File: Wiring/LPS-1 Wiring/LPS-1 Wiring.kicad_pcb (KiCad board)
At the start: 4 copper layers, 9 parts, among them J1 +12V Connector block, J2 Battery, J4 Solar charging unit, J5 Solar Panel, J6 GND Connector Block], J7 LPS-1 Monitoring Unit, J8 Fuse Block, SW2 Load Monitoring Control, SW3 Battery Kill Switch

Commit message: Chagnes to the panel layout
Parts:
- moved J8 75.8 mm to (644.7, 338.7)
- moved J1 62.3 mm to (586.8, 440.0)
- moved J6 62.3 mm to (607.7, 440.0)
- moved J2 49.0 mm to (537.6, 530.9), turned to -90 degrees
- moved J4 35.5 mm to (557.2, 357.7)
- moved J5 13.1 mm to (563.4, 219.3)
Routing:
- net unconnected-(J6-Pin_2-Pad6): track 219.3 -> 0.00 mm
- net unconnected-(J6-Pin_2-Pad2): track 0.00 -> 201.4 mm
- net /Lamp 11.2W: track 181.4 -> 253.0 mm
- net Net-(SW3B-A): track 111.8 -> 177.0 mm
- net Net-(SW2A-B): track 106.0 -> 168.6 mm
- net Net-(SW3A-A): track 85.9 -> 148.0 mm
- net Net-(J7-Pin_2): track 228.6 -> 277.5 mm
- net Net-(J2-Pin_1): track 110.5 -> 154.4 mm
- net /SP+: track 120.0 -> 145.9 mm
- net Net-(J2-Pin_2): track 166.3 -> 191.8 mm
- net /SP-: track 120.9 -> 144.9 mm
- net Net-(J8-COMM): track 273.7 -> 295.5 mm
- net Net-(J4-Pin_2): track 72.7 -> 93.1 mm
- net Net-(J4-Pin_1): track 79.3 -> 86.5 mm

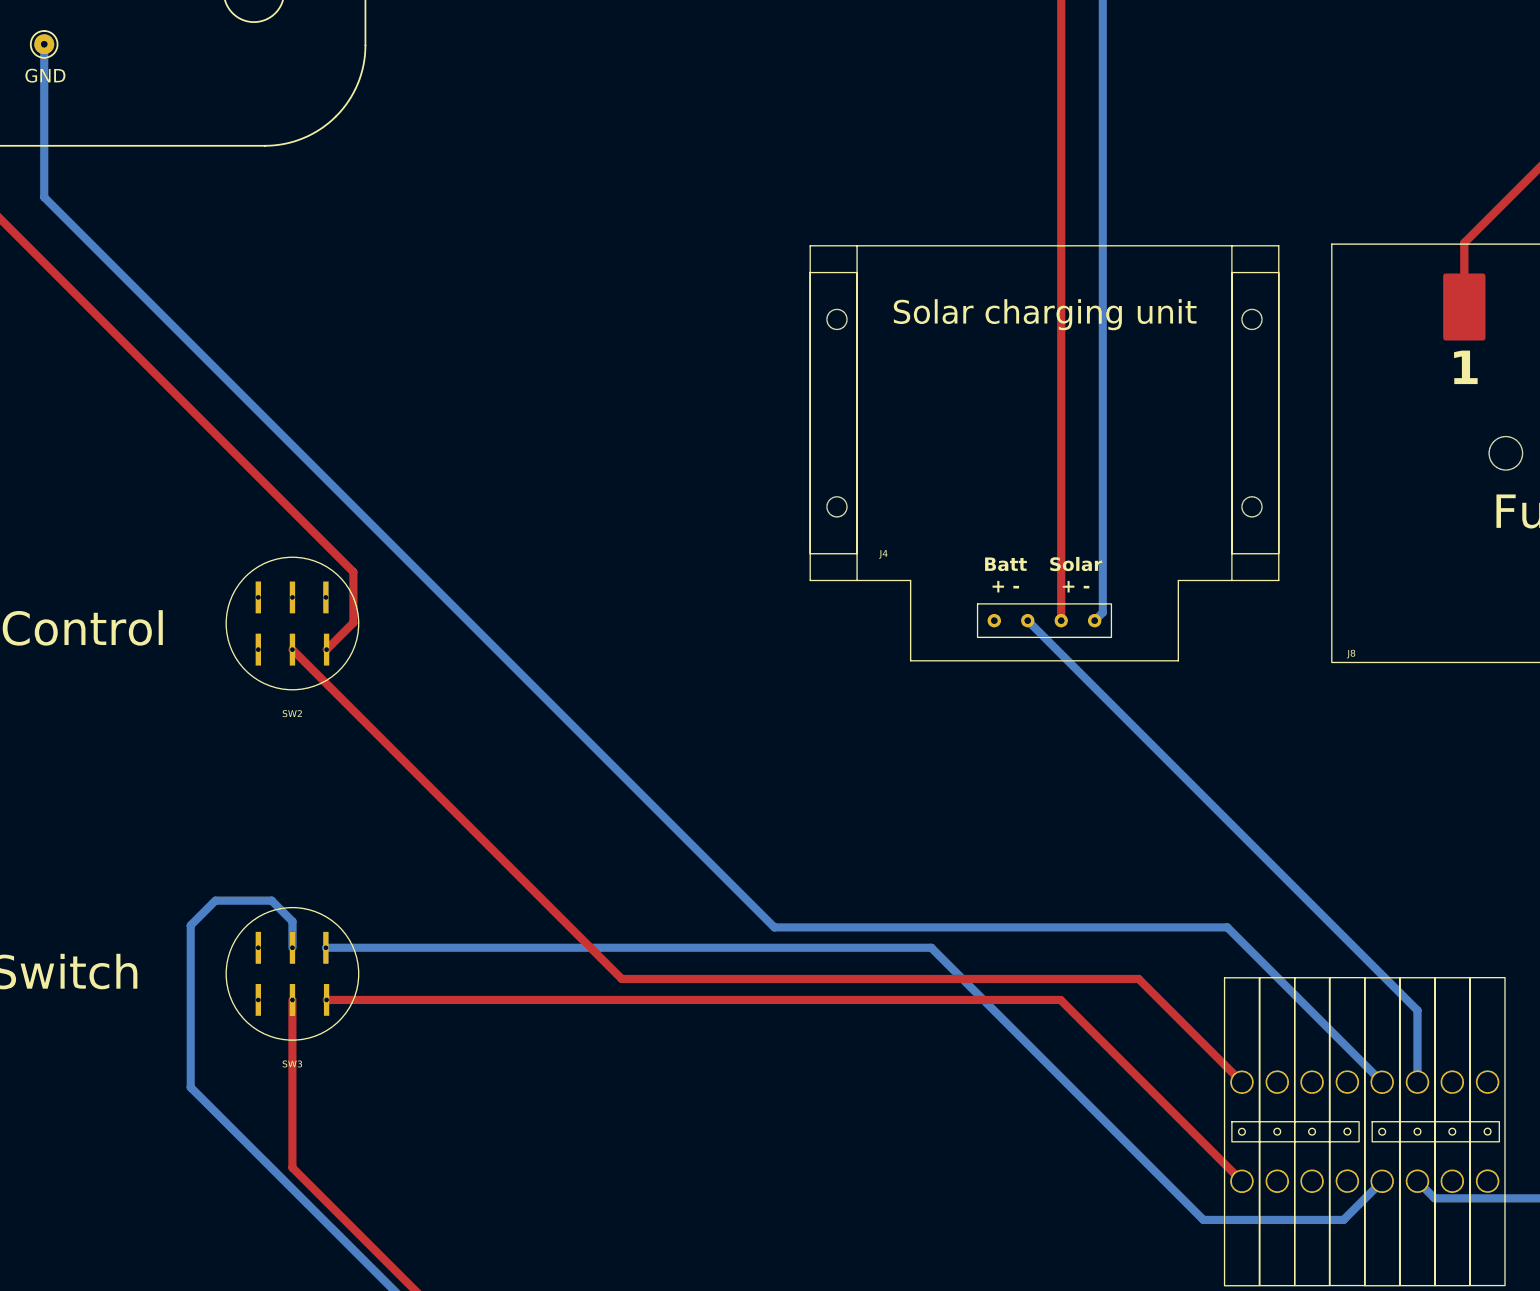
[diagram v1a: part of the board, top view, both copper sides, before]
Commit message: Moved the design to KiCad 10
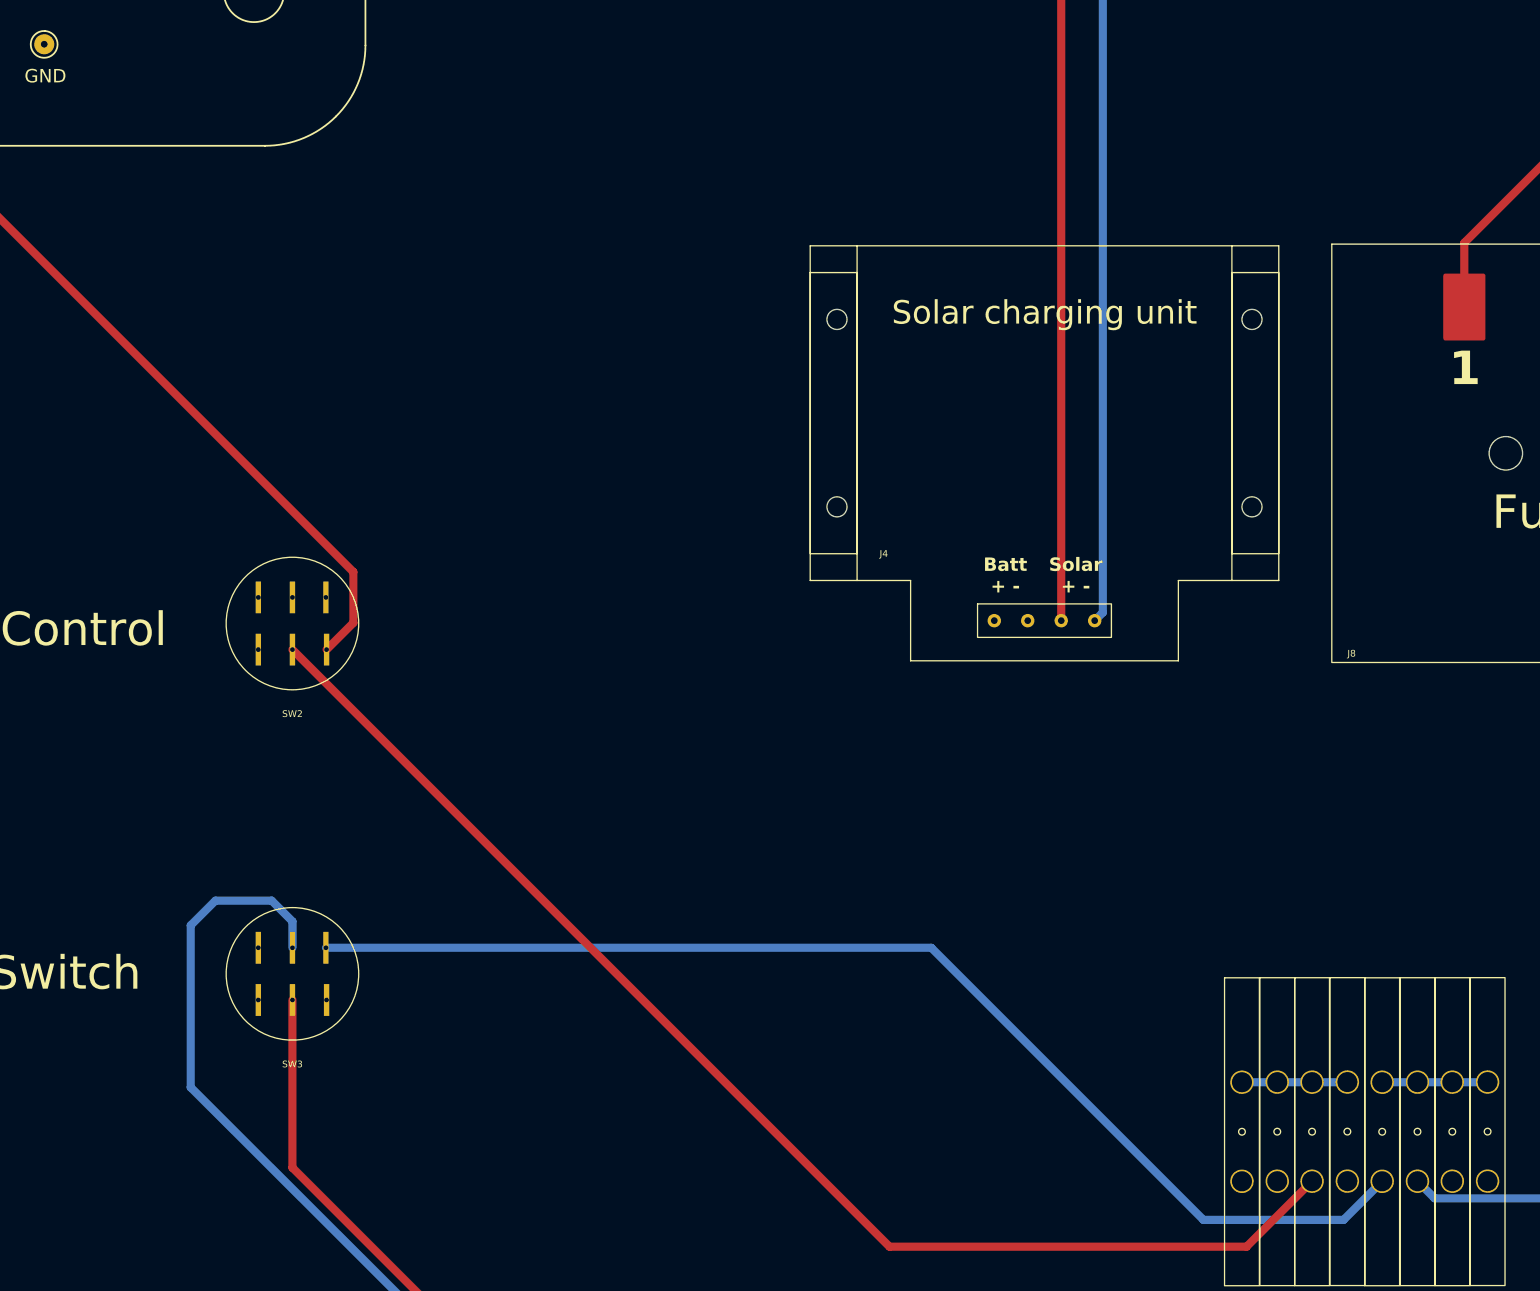
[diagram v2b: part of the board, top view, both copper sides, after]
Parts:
- J1, J6: footprint Wiring:Degson_04_Bridged-PC2.5-01P-11-00AH-1_5.2 -> Wiring:Degson_04_Bridged-PC2.5-01P-11-00AH-1_5.2_H
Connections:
- net /Lamp 11.2W renamed /Lamp +ve
- J1 pad 2: unconnected-(J1-Pin_2-Pad2) -> Net-(J4-Pin_1)
- J1 pad 3: unconnected-(J1-Pin_1-Pad3) -> Net-(SW2A-B)
- J1 pad 5: unconnected-(J1-Pin_1-Pad5) -> Net-(J1-Pin_1-Pad5)
- J1 pad 6: unconnected-(J1-Pin_2-Pad6) -> Net-(J1-Pin_1-Pad5)
- J1 pad 7: Net-(J4-Pin_1) -> Net-(J1-Pin_1-Pad5)
- J1 pad 8: Net-(SW2A-B) -> Net-(J1-Pin_1-Pad5)
- J4 pad 3: /SP+ -> unconnected-(J4-Pin_3-Pad3)
- J6 pad 2: unconnected-(J6-Pin_2-Pad2) -> Net-(J4-Pin_2)
- J6 pad 3: unconnected-(J6-Pin_1-Pad3) -> Net-(J7-Pin_2)
- J6 pad 4: unconnected-(J6-Pin_2-Pad4) -> /Lamp -Ve
- J6 pad 5: unconnected-(J6-Pin_1-Pad5) -> Net-(J6-Pin_1-Pad5)
- J6 pad 6: unconnected-(J6-Pin_2-Pad6) -> Net-(J6-Pin_1-Pad5)
- J6 pad 7: Net-(J4-Pin_2) -> Net-(J6-Pin_1-Pad5)
- J6 pad 8: Net-(J7-Pin_2) -> Net-(J6-Pin_1-Pad5)
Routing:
- net Net-(J4-Pin_2): track 93.1 -> 405.2 mm
- net unconnected-(J6-Pin_2-Pad2): track 201.4 -> 0.00 mm
- net Net-(J7-Pin_2): track 277.5 -> 374.6 mm
- net Net-(J4-Pin_1): track 86.5 -> 133.6 mm
- net Net-(SW2A-B): track 168.6 -> 193.3 mm
- net Net-(J1-Pin_1-Pad5): track 0.00 -> 15.8 mm
- net Net-(J6-Pin_1-Pad5): track 0.00 -> 15.8 mm
- net Net-(SW3A-A): track 148.0 -> 161.9 mm
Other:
- copper layers 4 -> 6

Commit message: Update to the connection block symols and footprints
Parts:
- removed the J6 at (607.7, 440.0)
- added J7: Block_Connector_04_b, Wiring:Degson_04_Bridged-PC2.5-01P-11-00AH-1_5.2, F.Cu at (606.9, 440.1)
- J1: value +12V Connector block -> Block_Connector_04_b; footprint Wiring:Degson_04_Bridged-PC2.5-01P-11-00AH-1_5.2_H -> Wiring:Degson_04_Bridged-PC2.5-01P-11-00AH-1_5.2
- moved J1 1.28 mm to (585.5, 440.0)
- renumbered J4 to J3, J5 to J4, J7 to J5, J8 to J6, SW3 to SW1
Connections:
- net Net-(J7-Pin_1) renamed /LPS_1_LOAD+
- net Net-(J7-Pin_3) renamed /LPS_1_LOAD-
- net Net-(SW3A-A) renamed /BAT+
- J1 pad 2: Net-(J4-Pin_1) -> unconnected-(J1-Pad2)
- J1 pad 3: Net-(SW2A-B) -> unconnected-(J1-Pad3)
- J1 pad 5: Net-(J1-Pin_1-Pad5) -> unconnected-(J1-Pad5)
- J1 pad 6: Net-(J1-Pin_1-Pad5) -> /CHRG+
- J1 pad 7: Net-(J1-Pin_1-Pad5) -> /LOAD
- J1 pad 8: Net-(J1-Pin_1-Pad5) -> unconnected-(J1-Pad8)
- J3 pad 1: Net-(J4-Pin_1) -> /CHRG+
- J3 pad 2: Net-(J4-Pin_2) -> /CHRG-
- J3 pad 3: unconnected-(J4-Pin_3-Pad3) -> /SP+
- J5 pad 2: Net-(J7-Pin_2) -> /LPS_1_GND
- SW1 pad 4: Net-(SW3B-A) -> /BAT-
- SW2 pad 2: Net-(SW2A-B) -> /LOAD
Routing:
- net Net-(J4-Pin_2): track 405.2 -> 0.00 mm
- net Net-(J7-Pin_2): track 374.6 -> 0.00 mm
- net /LPS_1_GND: track 0.00 -> 277.0 mm
- net /Lamp -Ve: track 0.00 -> 201.8 mm
- net Net-(SW2A-B): track 193.3 -> 0.00 mm
- net /LOAD: track 0.00 -> 178.2 mm
- net Net-(SW3B-A): track 177.0 -> 0.00 mm
- net /BAT-: track 0.00 -> 169.0 mm
- net Net-(J4-Pin_1): track 133.6 -> 0.00 mm
- net /CHRG-: track 0.00 -> 99.2 mm
- net /CHRG+: track 0.00 -> 88.1 mm
- net Net-(J1-Pin_1-Pad5): track 15.8 -> 0.00 mm
- net Net-(J6-Pin_1-Pad5): track 15.8 -> 0.00 mm
- net /BAT+: track 161.9 -> 161.2 mm

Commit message: Updated the wiring diagram
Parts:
- removed J5: LPS-1 Monitoring Unit, Wiring:LPS-1
- removed J6: Fuse Block, Wiring:FUSE_BLOCK_TRU_COMPONENTS-TC-9070396
- removed SW1: Battery Kill Switch, Wiring:SW_101_TC-R13-244D-02
- added F1: Chrg Fuse, Connector_PinHeader_2.54mm:PinHeader_1x02_P2.54mm_Vertical, F.Cu at (547.6, 380.2)
- added J10: GND Block, Wiring:Degson_04_Bridged-PC2.5-01P-11-00AH-1_5.2, F.Cu at (666.5, 442.4)
- added J11: Block_Connector_01_b, Wiring:Degson_01_PC2.5-01P-11-00AH-1_5.2, F.Cu at (525.8, 442.4)
- added J12: Block_Connector_01_b, Wiring:Degson_01_PC2.5-01P-11-00AH-1_5.2, F.Cu at (534.7, 442.4)
- added J13: Block_Connector_01_b, Wiring:Degson_01_PC2.5-01P-11-00AH-1_5.2, F.Cu at (635.8, 442.6)
- added J14: Block_Connector_01_b, Wiring:Degson_01_PC2.5-01P-11-00AH-1_5.2, F.Cu at (560.4, 442.4)
- added J15: Block_Connector_01_b, Wiring:Degson_01_PC2.5-01P-11-00AH-1_5.2, F.Cu at (642.1, 442.6)
- added J16: Block_Connector_01_b, Wiring:Degson_01_PC2.5-01P-11-00AH-1_5.2, F.Cu at (567.5, 442.4)
- added J17: Battery, Connector_PinHeader_2.54mm:PinHeader_1x02_P2.54mm_Vertical, F.Cu at (515.7, 513.8)
- added J20: Block_Connector_01_b, Wiring:Degson_01_PC2.5-01P-11-00AH-1_5.2, F.Cu at (616.3, 442.4)
- added J22: Pwr Block, Wiring:Degson_04_Bridged-PC2.5-01P-11-00AH-1_5.2, F.Cu at (583.3, 442.5)
- added J8: Fuse Block, Wiring:FUSE_BLOCK_TRU_COMPONENTS-TC-9070396, F.Cu at (647.7, 314.5)
- added J9: Solar charging unit, Wiring:H-TRONIC Solar-Lageregler, F.Cu at (559.4, 336.0)
- added LA1: Lamp, Connector_PinHeader_2.54mm:PinHeader_1x02_P2.54mm_Vertical, F.Cu at (298.6, 260.6)
- added LA2: Lamp, Connector_PinHeader_2.54mm:PinHeader_1x02_P2.54mm_Vertical, F.Cu at (680.3, 379.9)
- added SW3: ~, Wiring:TruComponents_SW_LAS0, F.Cu at (630.1, 379.1)
- J1: value Block_Connector_04_b -> Solar Panel; footprint Wiring:Degson_04_Bridged-PC2.5-01P-11-00AH-1_5.2 -> Connector_PinHeader_2.54mm:PinHeader_1x02_P2.54mm_Vertical
- J2: value Battery -> LPS-1 Monitoring Unit; footprint Connector_PinHeader_2.54mm:PinHeader_1x02_P2.54mm_Vertical -> Wiring:LPS-1
- J3: value Solar charging unit -> Block_Connector_01_b; footprint Wiring:H-TRONIC Solar-Lageregler -> Wiring:Degson_01_PC2.5-01P-11-00AH-1_5.2
- J4: value Solar Panel -> Block_Connector_01_b; footprint Connector_PinHeader_2.54mm:PinHeader_1x02_P2.54mm_Vertical -> Wiring:Degson_01_PC2.5-01P-11-00AH-1_5.2
- J7: value Block_Connector_04_b -> Block_Connector_01_b; footprint Wiring:Degson_04_Bridged-PC2.5-01P-11-00AH-1_5.2 -> Wiring:Degson_01_PC2.5-01P-11-00AH-1_5.2
- SW2: value Load Monitoring Control -> TRU Components NO; footprint Wiring:SW_101_TC-R13-244D-02 -> Wiring:TruComponents_SW_LAS0_1
- moved J1 334.8 mm to (367.1, 186.2), turned to 90 degrees
- moved J4 224.0 mm to (543.2, 442.4), turned to 0 degrees
- moved SW2 146.0 mm to (590.0, 380.2)
- moved J2 140.6 mm to (660.7, 598.8), turned to 0 degrees
- moved J3 84.8 mm to (553.0, 442.4)
- moved J7 3.80 mm to (609.9, 442.4)
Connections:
- J1 pad 1: /BAT+ -> /SOL-
- J1 pad 2: unconnected-(J1-Pad2) -> /SOL+
- J2 pad 1: Net-(J2-Pin_1) -> /MON+
- J2 pad 2: Net-(J2-Pin_2) -> /MON-
- J3 pad 1: /CHRG+ -> /SOL-
- J3 pad 2: /CHRG- -> /SOL_CHRG-
- J4 pad 1: /SP+ -> /SOL+
- J4 pad 2: /SP- -> /SOL_CHRG+
- J7 pad 1: unconnected-(J7-Pad1) -> /MON_LOAD
- J7 pad 2: unconnected-(J7-Pad2) -> /LOAD+
- SW2 pad 1: /LPS_1_LOAD+ -> Net-(SW2-11)
- SW2 pad 2: /LOAD -> /BATT+
- SW2 pad 3: Net-(J6-COMM) -> Net-(SW2-23)
- SW2 pad 4: Net-(J6-COMM) -> -VDC
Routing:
- net /SOL-: track 0.00 -> 986.6 mm
- net /SOL+: track 0.00 -> 969.7 mm
- net /Lamp -Ve: track 201.8 -> 1096.4 mm
- net /Lamp +ve: track 253.0 -> 1111.2 mm
- net /A Lamp +ve: track 0.00 -> 387.6 mm
- net /SYSTEM_PWR: track 0.00 -> 376.7 mm
- net /MON+: track 0.00 -> 329.5 mm
- net /Socket 12V: track 0.00 -> 322.9 mm
- net Net-(J6-COMM): track 295.5 -> 0.00 mm
- net /MON_LOAD: track 0.00 -> 293.8 mm
- net /LPS_1_GND: track 277.0 -> 0.00 mm
- net /PWR-COMM: track 0.00 -> 267.8 mm
- net /MON-: track 0.00 -> 255.0 mm
- net /SOL_CHRG-: track 0.00 -> 226.1 mm
- net /SOL_CHRG+: track 0.00 -> 212.4 mm
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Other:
- copper layers 6 -> 32
- board text added: "Battery"
- board text added: "Battery Kill"
- board text added: "Power Swap"

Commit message: Refactored the reference numbering
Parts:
- SK1: renamed from LA2; value Lamp -> Socket
- renumbered J11 to J1, J13 to J10, J15 to J11, J10 to J12, J17 to J13, J8 to J14, J1 to J15, J9 to J16, J2 to J17, J12 to J2, J4 to J3, J3 to J4, J14 to J5, J16 to J6, J22 to J7, J7 to J8, J20 to J9
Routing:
- net /SYSTEM_PWR: track 376.7 -> 364.2 mm
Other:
- board text added: "1.1"
- board text added: "1.2"
- board text added: "10.1"
- board text added: "10.2"
- board text added: "11.1"
- board text added: "11.2"
- board text added: "11.5"
- board text added: "12.1"
- board text added: "12.2"
- board text added: "12.3"
- board text added: "12.4"
- board text added: "12.6"
- board text added: "12.7"
- board text added: "12.8"
- board text added: "2.1"
- board text added: "2.2"
- board text added: "3.1"
- board text added: "3.2"
- board text added: "4.1"
- board text added: "4.2"
- board text added: "5.1"
- board text added: "5.2"
- board text added: "6.1"
- board text added: "7.1"
- board text added: "7.2"
- board text added: "7.3"
- board text added: "7.4"
- board text added: "7.6"
- board text added: "7.7"
- board text added: "7.8"
- board text added: "8.1"
- board text added: "8.2"
- board text added: "9.1"
- board text added: "9.2"

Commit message: Refactored the nomenclature for non-connector components
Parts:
- renumbered J13 to B1, J14 to FB1, J17 to LPS1, J16 to SC1, J15 to SP1

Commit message: Updates to the wriging layout
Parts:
- added J10: Block_Connector_01_b, Wiring:Degson_01_PC2.5-01P-11-00AH-1_5.2, F.Cu at (622.6, 442.4)
- added J11: Block_Connector_01_b, Wiring:Degson_01_PC2.5-01P-11-00AH-1_5.2, F.Cu at (629.2, 442.4)
- added J9: Block_Connector_01_b, Wiring:Degson_01_PC2.5-01P-11-00AH-1_5.2, F.Cu at (616.1, 442.4)
- LPS1: footprint Wiring:LPS-1 -> Wiring:LPS-1_EXT_PWR
- moved SP1 79.1 mm to (427.0, 237.9)
- moved LA1 77.2 mm to (365.6, 299.1)
- moved J12 21.2 mm to (637.5, 442.4)
- moved J101 13.1 mm to (648.9, 442.4)
- moved J102 13.1 mm to (655.2, 442.4)
- moved LPS1 0.34 mm to (660.4, 598.7)
- renumbered J10 to J101, J11 to J102, J9 to J12, J12 to J500
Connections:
- net /MON- renamed /LPS-GND
- net /PWR-COMM renamed /PWR-COMM-B
- F1 pad 1: /CHRG+ -> /SYSTEM_PWR
- FB1 pad 2: /Socket 12V -> /LPS-12V
- FB1 pad 3: unconnected-(FB1-Pad3) -> /Socket 12V
- J12 pad 1: /SYSTEM_PWR -> /PWR-COMM-A
- J7 pad 3: /MON+ -> unconnected-(J7-Pad3)
- J7 pad 4: unconnected-(J7-Pad4) -> /PWR-COMM-A
- J7 pad 5: /BATT_DIRECT -> unconnected-(J7-Pad5)
- J8 pad 1: /MON_LOAD -> /VIN-
- LPS1 pad 1: /MON+ -> Net-(LPS1-Pin_1)
- LPS1 pad 3: /MON_LOAD -> /VIN+
- SW3 pad 1: /LOAD+ -> Net-(SW3A-11)
- SW3 pad 3: /BATT_DIRECT -> /LOAD+
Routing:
- net /LPS-12V: track 0.00 -> 360.9 mm
- net /VIN-: track 0.00 -> 334.1 mm
- net /MON+: track 329.5 -> 0.00 mm
- net Net-(LPS1-Pin_1): track 0.00 -> 299.6 mm
- net /VIN+: track 0.00 -> 297.1 mm
- net /MON_LOAD: track 293.8 -> 0.00 mm
- net /SYSTEM_PWR: track 364.2 -> 157.2 mm
- net /Lamp -Ve: track 1096.4 -> 989.4 mm
- net /Lamp +ve: track 1111.2 -> 1007.0 mm
- net /PWR-COMM-A: track 0.00 -> 83.4 mm
- net /SOL+: track 969.7 -> 893.1 mm
- net /SOL-: track 986.6 -> 910.1 mm
- net /BATT_DIRECT: track 74.2 -> 0.00 mm
- net Net-(SW3A-11): track 0.00 -> 58.2 mm
- net /Socket 12V: track 322.9 -> 283.4 mm
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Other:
- board text added: "101.1"
- board text added: "101.2"
- board text added: "102.1"
- board text added: "102.2"
- board text added: "500.1"
- board text added: "500.2"
- board text added: "500.3"
- board text added: "500.4"
- board text added: "500.5"
- board text added: "500.6"
- board text added: "500.7"
- board text added: "500.8"
- board text added: "6.2"
- board text added: "F1.1"
- board text added: "Vin+ (Load)"
- board text added: "Vout+ (Load)"
- board text removed: "12.3"
- board text removed: "12.4"
- board text removed: "12.6"
- board text removed: "12.8"
- board text removed: "Vin- (Load)"

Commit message: Reconfigured the LPS-1 wiring
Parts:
- removed the J10 at (622.6, 442.4)
- added J8: Block_Connector_01_b, Wiring:Degson_01_PC2.5-01P-11-00AH-1_5.2, F.Cu at (604.9, 442.4)
- added J9: Block_Connector_01_b, Wiring:Degson_01_PC2.5-01P-11-00AH-1_5.2, F.Cu at (611.2, 442.4)
- moved J10 6.85 mm to (616.8, 442.4)
- moved J11 6.85 mm to (623.0, 442.4)
- moved F1 2.44 mm to (550.0, 380.2), turned to -90 degrees
- renumbered J8 to J10, J9 to J11, J11 to J12, J12 to J13
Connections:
- F1 pad 1: /SYSTEM_PWR -> /SYSTEM_PWR_1
- F1 pad 2: Net-(F1-Pad2) -> /SYSTEM_PWR
- J10 pad 2: /LOAD+ -> Net-(SW3B-24)
- J11 pad 2: /CHRG+ -> /Vin+_S1
- J500 pad 7: Net-(SW3B-12) -> unconnected-(J500-Pad7)
- J500 pad 8: unconnected-(J500-Pad8) -> -VDC
- J7 pad 8: Net-(F1-Pad2) -> /SYSTEM_PWR
- SW3 pad 1: Net-(SW3A-11) -> /CHRG+
- SW3 pad 2: /SYSTEM_PWR -> /SYSTEM_PWR_2
- SW3 pad 3: /LOAD+ -> /CHRG+
- SW3 pad 4: /SYSTEM_PWR -> /Vin+_S1
- SW3 pad 5: -VDC -> unconnected-(SW3B-11-Pad5)
- SW3 pad 6: Net-(SW3B-12) -> unconnected-(SW3B-12-Pad6)
- SW3 pad 7: -VDC -> /SYSTEM_PWR_3
- SW3 pad 8: Net-(SW3B-12) -> Net-(SW3B-24)
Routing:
- net /SYSTEM_PWR_3: track 0.00 -> 345.0 mm
- net /CHRG+: track 202.2 -> 315.2 mm
- net /SYSTEM_PWR_1: track 0.00 -> 103.4 mm
- net Net-(SW3B-12): track 90.7 -> 0.00 mm
- net Net-(F1-Pad2): track 80.0 -> 0.00 mm
- net /SYSTEM_PWR: track 157.2 -> 83.9 mm
- net /SYSTEM_PWR_2: track 0.00 -> 70.7 mm
- net /LOAD+: track 69.9 -> 0.00 mm
- net /Vin+_S1: track 0.00 -> 68.9 mm
- net Net-(SW3B-24): track 0.00 -> 67.1 mm
- net Net-(SW3A-11): track 58.2 -> 0.00 mm
- net /VIN-: track 334.1 -> 284.5 mm
- net -VDC: track 81.5 -> 115.6 mm
- net /VIN+: track 297.1 -> 281.9 mm
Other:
- board text added: "13.1"
- board text added: "13.2"
